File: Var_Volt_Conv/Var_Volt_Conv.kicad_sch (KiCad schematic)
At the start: 0 parts

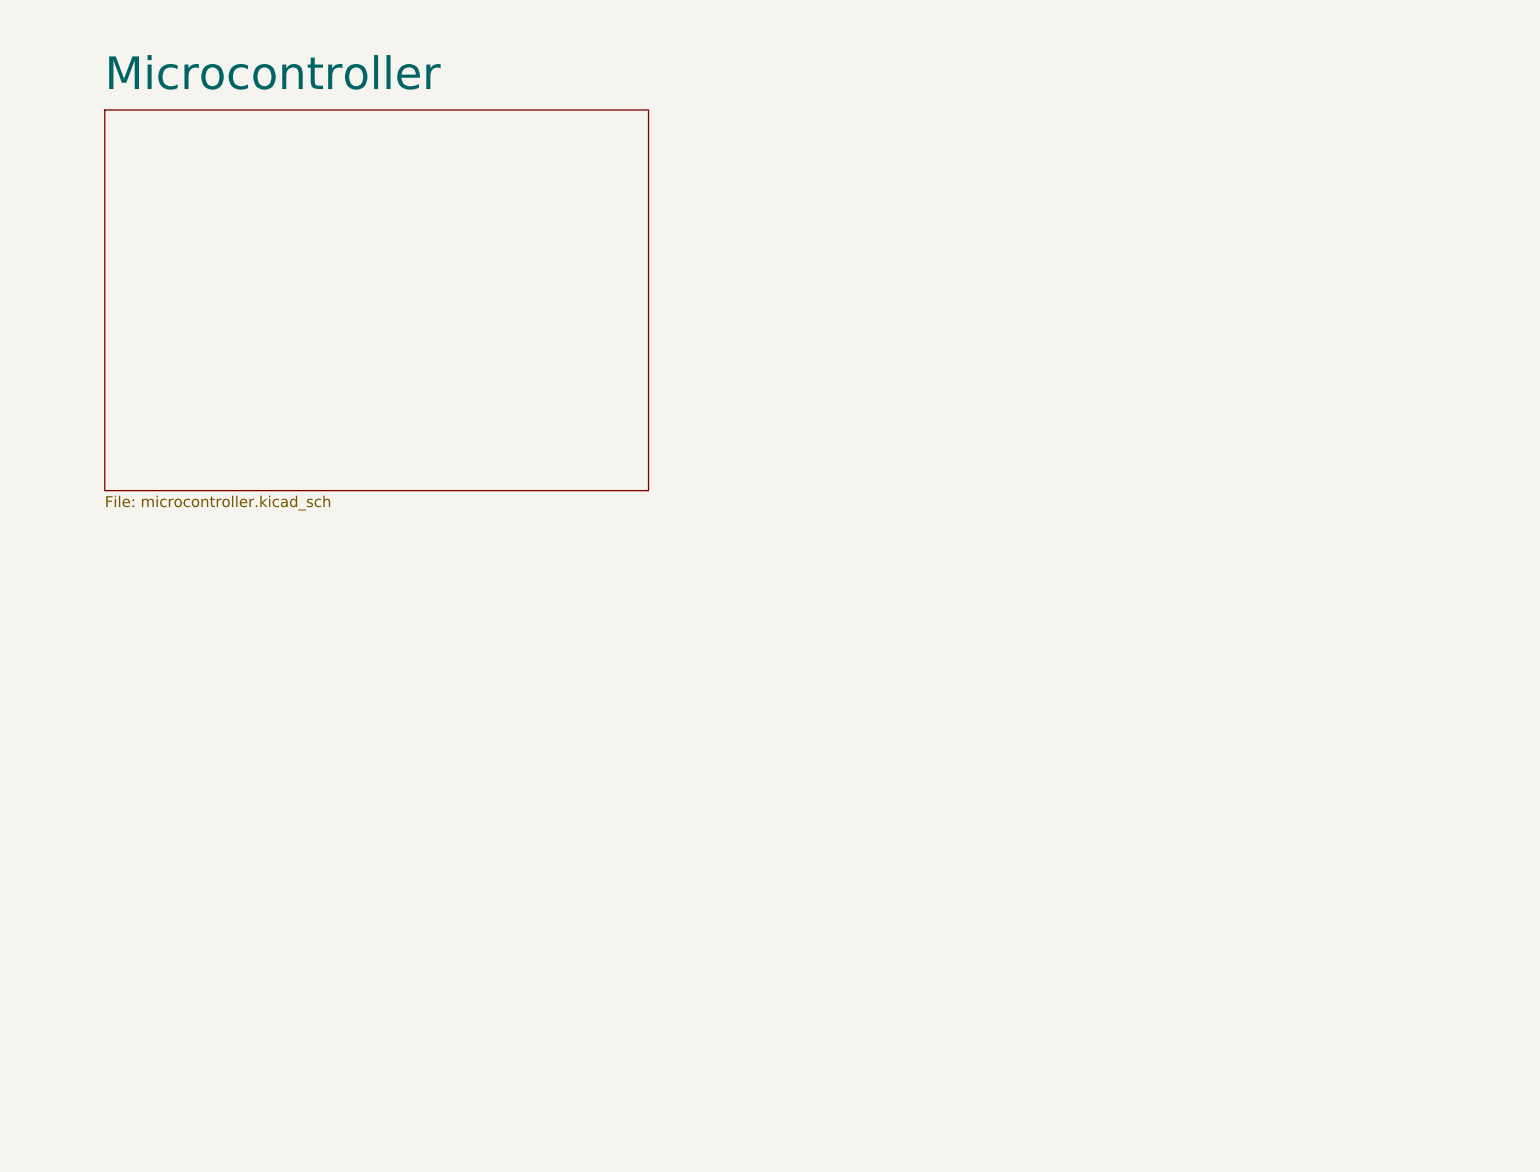
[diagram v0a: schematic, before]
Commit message: Add 3.3V buck Converter TPS61272DSGT
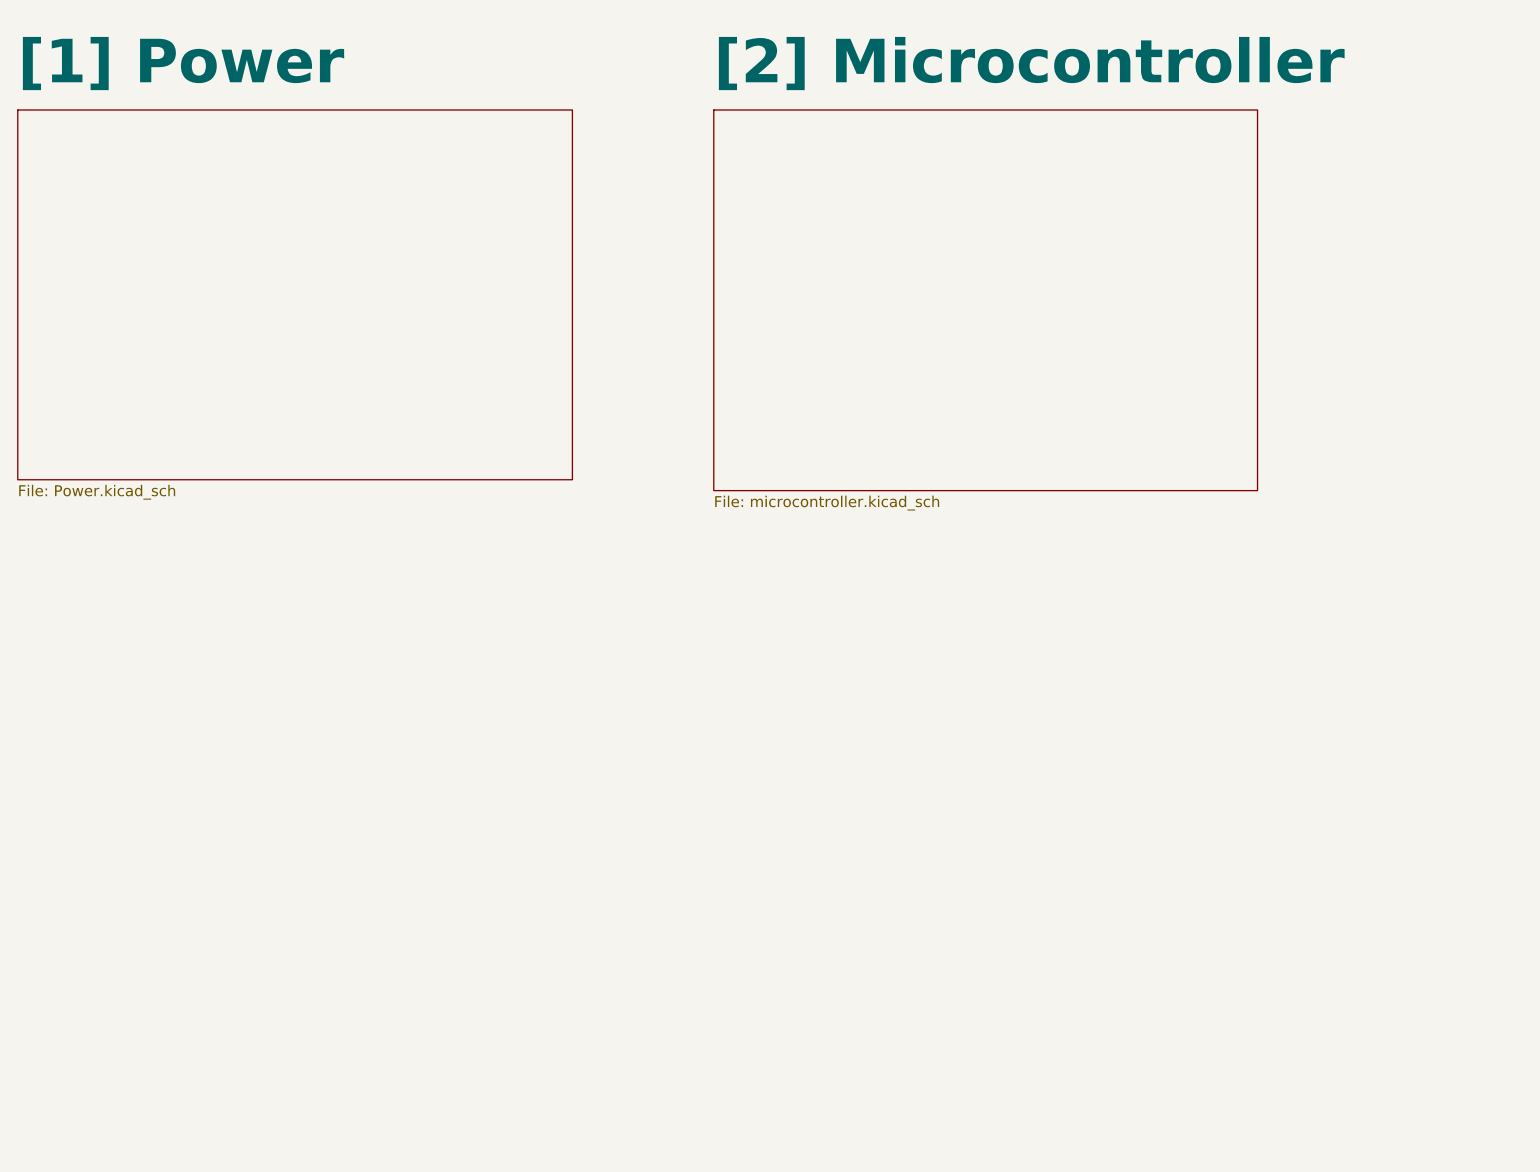
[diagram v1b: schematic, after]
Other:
- sheet Microcontroller renamed [2] Microcontroller
- added sheet [1] Power (Power.kicad_sch)
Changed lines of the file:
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@@
 	(paper "A4")
 	(sheet
-		(at 36.83 29.21)
+		(at 26.67 29.21)
+		(size 64.77 43.18)
+		(fields_autoplaced yes)
+		(stroke
+			(width 0.1524)
+			(type solid)
+		)
+		(fill
+			(color 0 0 0 0.0000)
+		)
+		(property "Sheetname" "[1] Power"
+			(at 26.67 26.5934 0)
+			(effects
+				(font
+					(size 5.08 5.08)
+					(thickness 1.016)
+					(bold yes)
+				)
+				(justify left bottom)
+			)
+		)
+		(property "Sheetfile" "Power.kicad_sch"
+			(at 26.67 72.9746 0)
+			(effects
+				(font
+					(size 1.27 1.27)
+				)
+				(justify left top)
+			)
+		)
+		(instances
+			(project "Var_Volt_Conv"
+				(path "/7c9580d6-c22f-4506-b9c3-9272e882c9fb"
+					(page "3")
+				)
+			)
+		)
+	)
+	(sheet
+		(at 107.95 29.21)
 		(size 63.5 44.45)
 		(fields_autoplaced yes)
@@
 			(color 0 0 0 0.0000)
 		)
-		(property "Sheetname" "Microcontroller"
-			(at 36.83 27.2284 0)
+		(property "Sheetname" "[2] Microcontroller"
+			(at 107.95 26.5934 0)
 			(effects
 				(font
-					(size 3.81 3.81)
+					(size 5.08 5.08)
+					(thickness 1.016)
+					(bold yes)
 				)
 				(justify left bottom)
@@
 		)
 		(property "Sheetfile" "microcontroller.kicad_sch"
-			(at 36.83 74.2446 0)
+			(at 107.95 74.2446 0)
 			(effects
 				(font

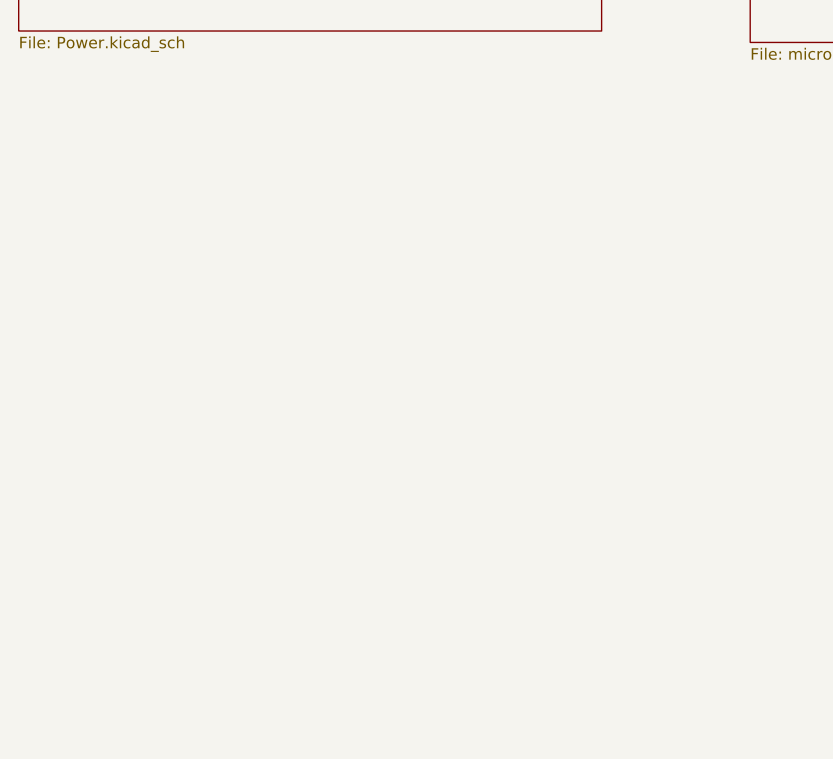
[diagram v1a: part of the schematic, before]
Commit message: Tidied up microcontoller schematic
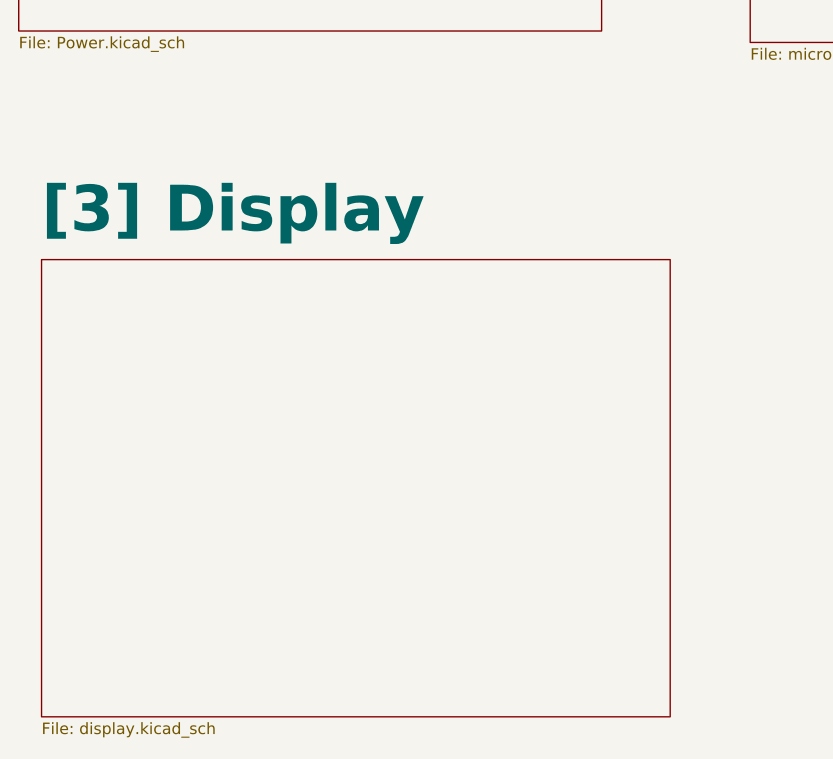
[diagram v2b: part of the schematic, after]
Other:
- added sheet [3] Display (display.kicad_sch)
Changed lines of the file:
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@@
+		)
+	)
+	(sheet
+		(at 29.21 97.79)
+		(size 69.85 50.8)
+		(fields_autoplaced yes)
+		(stroke
+			(width 0.1524)
+			(type solid)
+		)
+		(fill
+			(color 0 0 0 0.0000)
+		)
+		(property "Sheetname" "[3] Display"
+			(at 29.21 95.1734 0)
+			(effects
+				(font
+					(size 5.08 5.08)
+					(thickness 1.016)
+					(bold yes)
+				)
+				(justify left bottom)
+			)
+		)
+		(property "Sheetfile" "display.kicad_sch"
+			(at 29.21 149.1746 0)
+			(effects
+				(font
+					(size 1.27 1.27)
+				)
+				(justify left top)
+			)
+		)
+		(instances
+			(project "Var_Volt_Conv"
+				(path "/7c9580d6-c22f-4506-b9c3-9272e882c9fb"
+					(page "4")
+				)
+			)
 		)
 	)

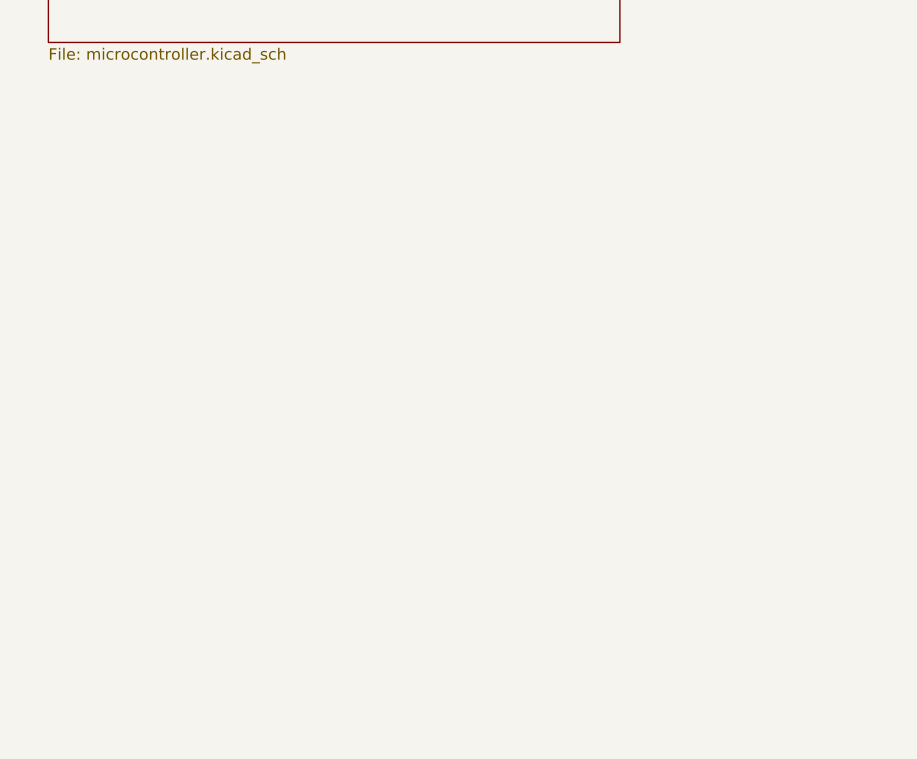
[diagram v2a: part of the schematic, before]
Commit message: Add Current-sense amps library, INA215-75V/V gain and INA213-50V/V gain symbols
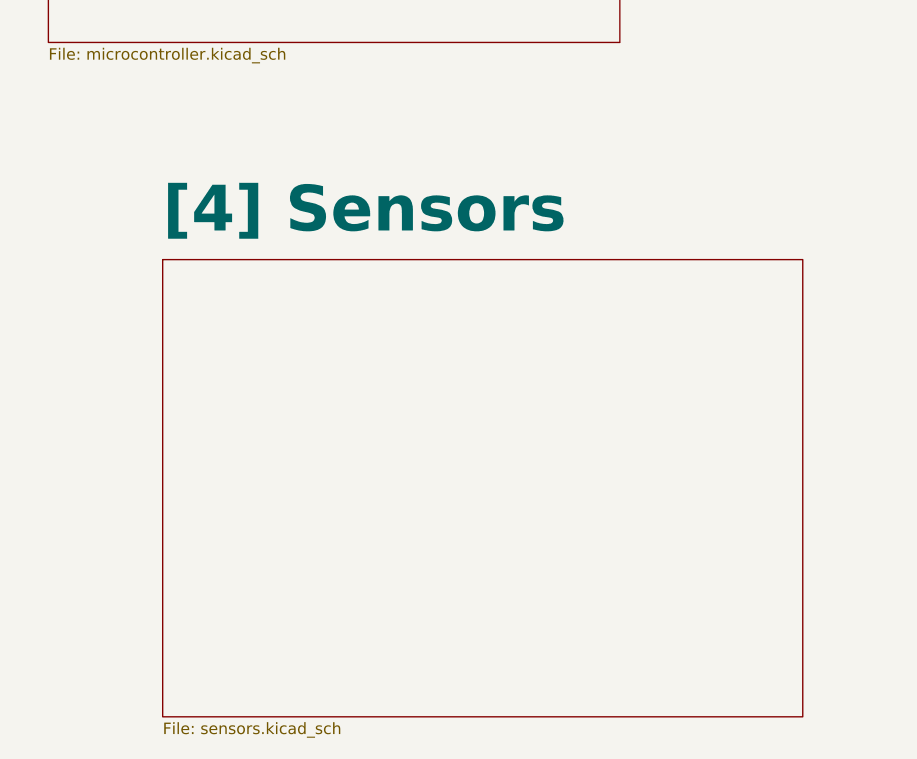
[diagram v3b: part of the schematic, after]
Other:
- added sheet [4] Sensors (sensors.kicad_sch)
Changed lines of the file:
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@@
+	)
+	(sheet
+		(at 120.65 97.79)
+		(size 71.12 50.8)
+		(fields_autoplaced yes)
+		(stroke
+			(width 0.1524)
+			(type solid)
+		)
+		(fill
+			(color 0 0 0 0.0000)
+		)
+		(property "Sheetname" "[4] Sensors"
+			(at 120.65 95.1734 0)
+			(effects
+				(font
+					(size 5.08 5.08)
+					(thickness 1.016)
+					(bold yes)
+				)
+				(justify left bottom)
+			)
+		)
+		(property "Sheetfile" "sensors.kicad_sch"
+			(at 120.65 149.1746 0)
+			(effects
+				(font
+					(size 1.27 1.27)
+				)
+				(justify left top)
+			)
+		)
+		(instances
+			(project "Var_Volt_Conv"
+				(path "/7c9580d6-c22f-4506-b9c3-9272e882c9fb"
+					(page "5")
+				)
+			)
+		)
 	)
 	(sheet

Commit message: Labeled subcircuits in PCB
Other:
- title: (none) -> Variable Voltage Controller
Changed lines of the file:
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@@
 	(generator_version "8.0")
 	(paper "A4")
+	(title_block
+		(title "Variable Voltage Controller")
+		(date "2025-02-02")
+		(rev "1.0")
+	)
 	(sheet
 		(at 26.67 29.21)
